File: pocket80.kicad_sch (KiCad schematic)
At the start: 4 parts

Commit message: HW: Start final placement
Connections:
- no-connect marks 0 -> 1
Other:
- moved on the sheet: H1, H2, H3, H4

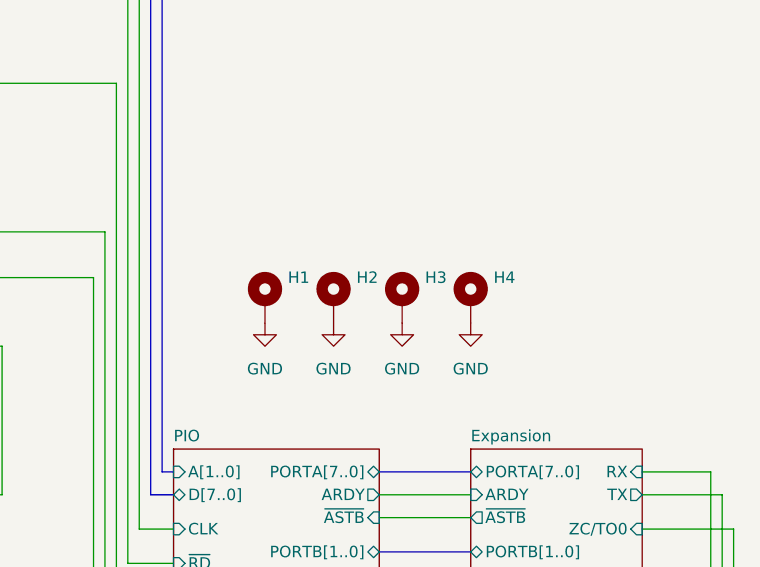
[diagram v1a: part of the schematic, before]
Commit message: HW: Fix mounting holes
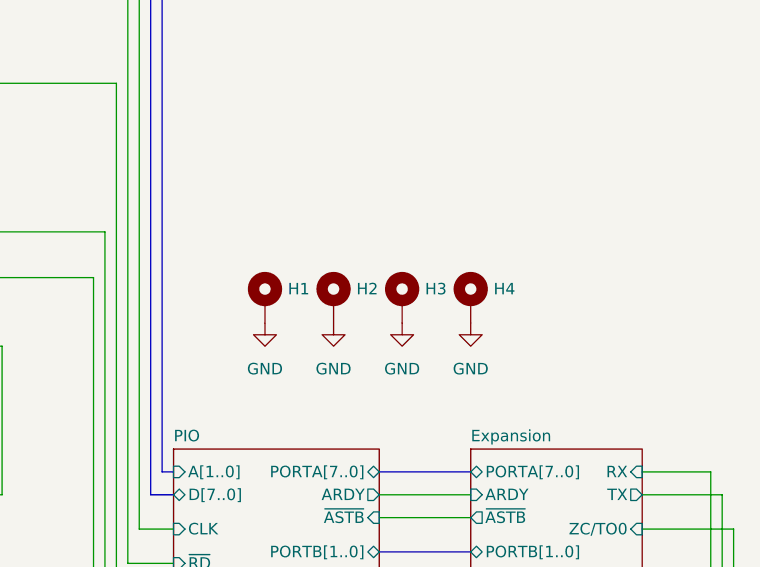
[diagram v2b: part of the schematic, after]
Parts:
- H1, H2, H3, H4: symbol Mechanical:MountingHole_Pad_MP -> Mechanical:MountingHole_Pad
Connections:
- net GND: now also H1.1, H2.1, H3.1, H4.1; no longer H1.MP, H2.MP, H3.MP, H4.MP
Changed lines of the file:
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@@
 	)
 	(symbol
-		(lib_id "Mechanical:MountingHole_Pad_MP")
+		(lib_id "Mechanical:MountingHole_Pad")
 		(at 228.6 81.28 0)
 		(unit 1)
@@
 		(fields_autoplaced yes)
 		(property "Reference" "H1"
-			(at 231.14 78.7399 0)
+			(at 231.14 80.0099 0)
 			(effects
 				(font
@@
 			)
 		)
-		(property "Description" "Mounting Hole with connection as pad named MP"
+		(property "Description" "Mounting Hole with connection"
 			(at 228.6 81.28 0)
 			(effects
@@
 			)
 		)
-		(pin "MP"
+		(pin "1"
 		)
 		(instances
@@
 	)
 	(symbol
-		(lib_id "Mechanical:MountingHole_Pad_MP")
+		(lib_id "Mechanical:MountingHole_Pad")
 		(at 251.46 81.28 0)
 		(unit 1)
@@
 		(fields_autoplaced yes)
 		(property "Reference" "H4"
-			(at 254 78.7399 0)
+			(at 254 80.0099 0)
 			(effects
 				(font
@@
 			)
 		)
-		(property "Description" "Mounting Hole with connection as pad named MP"
+		(property "Description" "Mounting Hole with connection"
 			(at 251.46 81.28 0)
 			(effects
@@
 			)
 		)
-		(pin "MP"
+		(pin "1"
 		)
 		(instances
@@
 	)
 	(symbol
-		(lib_id "Mechanical:MountingHole_Pad_MP")
+		(lib_id "Mechanical:MountingHole_Pad")
 		(at 243.84 81.28 0)
 		(unit 1)
@@
 		(fields_autoplaced yes)
 		(property "Reference" "H3"
-			(at 246.38 78.7399 0)
+			(at 246.38 80.0099 0)
 			(effects
 				(font
@@
 			)
 		)
-		(property "Description" "Mounting Hole with connection as pad named MP"
+		(property "Description" "Mounting Hole with connection"
 			(at 243.84 81.28 0)
 			(effects
@@
 			)
 		)
-		(pin "MP"
+		(pin "1"
 		)
 		(instances
@@
 	)
 	(symbol
-		(lib_id "Mechanical:MountingHole_Pad_MP")
+		(lib_id "Mechanical:MountingHole_Pad")
 		(at 236.22 81.28 0)
 		(unit 1)
@@
 		(fields_autoplaced yes)
 		(property "Reference" "H2"
-			(at 238.76 78.7399 0)
+			(at 238.76 80.0099 0)
 			(effects
 				(font
@@
 			)
 		)
-		(property "Description" "Mounting Hole with connection as pad named MP"
+		(property "Description" "Mounting Hole with connection"
 			(at 236.22 81.28 0)
 			(effects
@@
 			)
 		)
-		(pin "MP"
-		)
-		(instances
+		(pin "1"
+		)
+		(instances
